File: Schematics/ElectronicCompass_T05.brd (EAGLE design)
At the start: 100 x 80 mm, 59 parts, among them Q1 SPB80P06P, Q2 SPB80P06P, Q3 SPB80P06P, Q4 SPB80P06P, U1 ATMEGA32U4, X1 USBSMD

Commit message: Last minute changes to schematic before the layout begins
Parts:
- added TP26, TP27, TP28: TPTP06R, testpad:TP06R
- C12: value 1uF -> 10uF
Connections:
- new net N$37: Q3.1, U1.8
- new net N$38: TP26.TP, U1.32
- new net N$40: TP28.TP, U1.11
- net N$39: now also TP27.TP; no longer Q3.1
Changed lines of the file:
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@@
 <element name="Q1" library="transistor-fet" package="TO263" value="SPB80P06P" x="35.56" y="52.705"/>
 <element name="Q2" library="transistor-fet" package="TO263" value="SPB80P06P" x="25.4" y="55.245"/>
-<element name="C12" library="rcl" package="C0805" value="1uF" x="18.415" y="31.115"/>
+<element name="C12" library="rcl" package="C0805" value="10uF" x="18.415" y="31.115"/>
 <element name="G1" library="battery" package="SL-340/SM3.6V" value="SL340SM" x="85.09" y="30.48"/>
 <element name="C4" library="rcl" package="C0805" value="1uF" x="42.545" y="39.37"/>
@@
 <element name="U$1" library="LTC4067" package="DFN-12" value="LTC4067" x="-17.78" y="-89.535"/>
 <element name="C3" library="rcl" package="C0805" value="0.1uF" x="-19.05" y="-96.52"/>
+<element name="TP26" library="testpad" package="TP06R" value="TPTP06R" x="-20.32" y="-102.235">
+<attribute name="TP_SIGNAL_NAME" value="" x="-20.32" y="-102.235" size="1.778" layer="27" display="off"/>
+</element>
+<element name="TP27" library="testpad" package="TP06R" value="TPTP06R" x="-20.32" y="-105.41">
+<attribute name="TP_SIGNAL_NAME" value="" x="-20.32" y="-105.41" size="1.778" layer="27" display="off"/>
+</element>
+<element name="TP28" library="testpad" package="TP06R" value="TPTP06R" x="-20.32" y="-108.585">
+<attribute name="TP_SIGNAL_NAME" value="" x="-20.32" y="-108.585" size="1.778" layer="27" display="off"/>
+</element>
 </elements>
 <signals>
@@
 <wire x1="9.525" y1="-15.24" x2="55.92" y2="28.35" width="0" layer="19" extent="1-1"/>
 </signal>
-<signal name="N$39">
-<contactref element="U1" pad="22"/>
-<contactref element="Q3" pad="1"/>
-<wire x1="0.635" y1="-30.73" x2="60.92" y2="28.35" width="0" layer="19" extent="1-1"/>
-</signal>
 <signal name="N$27">
 <contactref element="U1" pad="30"/>
@@
 <wire x1="39.05" y1="47.625" x2="-18.53" y2="-90.885" width="0" layer="19" extent="1-1"/>
 </signal>
+<signal name="N$37">
+<contactref element="U1" pad="8"/>
+<contactref element="Q3" pad="1"/>
+<wire x1="0.635" y1="-30.73" x2="55.02" y2="30.75" width="0" layer="19" extent="1-1"/>
+</signal>
+<signal name="N$38">
+<contactref element="U1" pad="32"/>
+<contactref element="TP26" pad="TP"/>
+<wire x1="61.82" y1="33.75" x2="-20.32" y2="-102.235" width="0" layer="19" extent="1-1"/>
+</signal>
+<signal name="N$39">
+<contactref element="U1" pad="22"/>
+<contactref element="TP27" pad="TP"/>
+<wire x1="60.92" y1="28.35" x2="-20.32" y2="-105.41" width="0" layer="19" extent="1-1"/>
+</signal>
+<signal name="N$40">
+<contactref element="U1" pad="11"/>
+<contactref element="TP28" pad="TP"/>
+<wire x1="55.02" y1="29.25" x2="-20.32" y2="-108.585" width="0" layer="19" extent="1-1"/>
+</signal>
 </signals>

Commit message: Board layout changes
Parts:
- removed JP4: LOGO-SFENEW, SparkFun:SFE-NEW-WEBLOGO
- removed JP5: LOGO-SFESK, SparkFun:SFE-LOGO-FLAME
- moved TP25 135.8 mm to (5.08, 49.5)
- moved U$1 134.8 mm to (29.2, 36.8), turned to 270 degrees
- moved TP24 133.7 mm to (23.5, 47.6), flipped to the bottom, turned to 180 degrees
- moved TP23 133.0 mm to (21.6, 52.1), turned to 180 degrees
- moved C3 132.8 mm to (15.2, 31.8), turned to 180 degrees
- moved TP26 131.2 mm to (38.1, 15.2)
- moved TP28 128.7 mm to (29.2, 10.2)
- moved TP22 128.4 mm to (24.1, 50.2), turned to 180 degrees
- moved TP21 128.3 mm to (26.7, 52.7), turned to 180 degrees
- moved S2 127.8 mm to (8.89, 54.0), flipped to the bottom, turned to 90 degrees
- moved TP27 126.9 mm to (36.2, 8.26)
- moved C2 126.3 mm to (28.6, 29.2)
- moved TP19 123.8 mm to (31.8, 53.3), turned to 180 degrees
- moved TP20 123.2 mm to (29.2, 50.2), turned to 180 degrees
- moved TP17 119.6 mm to (34.3, 51.4), turned to 180 degrees
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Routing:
- added copper zone on layer 1, net GND
- added copper zone on layer 16, net GND
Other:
- board size 100 x 80 mm -> 63.2 x 61 mm

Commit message: board layout continued
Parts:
- moved R8 26.2 mm to (60.3, 15.2), turned to 270 degrees
- moved TP24 23.9 mm to (1.27, 38.7)
- moved C10 23.9 mm to (36.8, 38.7), turned to 0 degrees
- moved R6 22.3 mm to (36.2, 34.9), turned to 0 degrees
- moved R7 21.6 mm to (18.4, 2.54), turned to 90 degrees
- moved C4 19.3 mm to (27.3, 12.7), turned to 180 degrees
- moved C3 18.7 mm to (30.5, 21.0), turned to 90 degrees
- moved C12 16.5 mm to (30.5, 26.7)
- moved S2 15.4 mm to (6.99, 38.7), turned to 180 degrees
- moved S1 15.3 mm to (6.35, 27.9)
- moved R1 13.6 mm to (19.1, 12.7), turned to 90 degrees
- moved X1 8.35 mm to (6.35, 19.1)
- moved TP25 7.41 mm to (1.27, 43.2), flipped to the bottom, turned to 180 degrees
- moved C5 5.24 mm to (27.3, 40.0)
- moved R2 5.12 mm to (20.3, 15.9)
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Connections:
- net GND: no longer U$1.P13, U$1.P3
- net N$16: now also U$1.P10; no longer U$1.P9
- net N$4: no longer U$1.P1
- net N$5: now also U$1.P9; no longer U$1.P10
- net VCC: no longer U$1.P4, U$1.P5

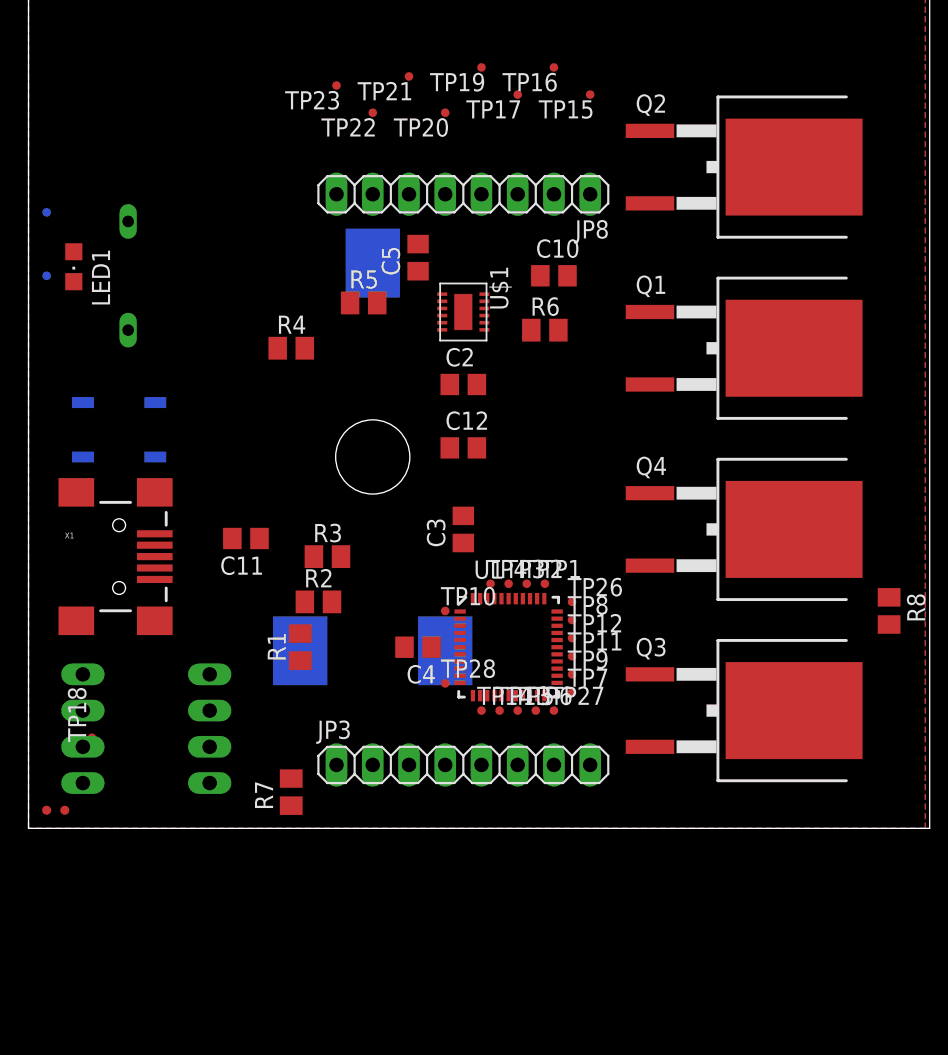
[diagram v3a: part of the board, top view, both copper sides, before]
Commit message: New transistors
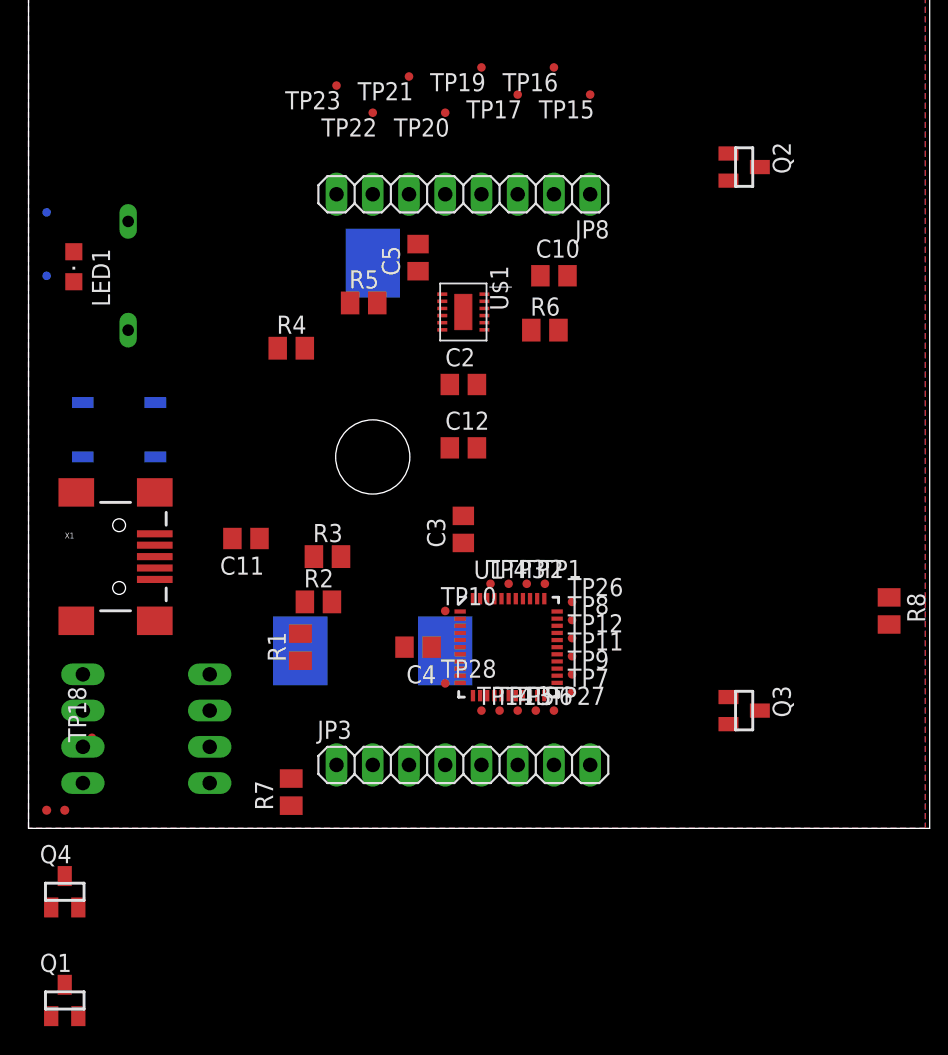
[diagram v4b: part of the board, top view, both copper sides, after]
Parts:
- Q1, Q2, Q3, Q4: value SPB80P06P -> FDN360P; device transistor-fet:TO263 -> transistor-power:SUPER-SOT3
- moved Q1 66.0 mm to (2.54, -12.1), turned to 0 degrees
- moved Q4 54.0 mm to (2.54, -4.45), turned to 0 degrees
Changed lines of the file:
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@@
 <element name="C11" library="rcl" package="C0805" value="1uF" x="15.24" y="20.32" rot="R180"/>
 <element name="LED1" library="led" package="CHIPLED_0805" value="1" x="3.175" y="39.37" rot="R180"/>
-<element name="Q1" library="transistor-fet" package="TO263" value="SPB80P06P" x="50.165" y="33.655" rot="R270"/>
-<element name="Q2" library="transistor-fet" package="TO263" value="SPB80P06P" x="50.165" y="46.355" rot="R270"/>
+<element name="Q2" library="transistor-power" package="SUPER-SOT3" value="FDN360P" x="50.165" y="46.355" rot="R270"/>
 <element name="C12" library="rcl" package="C0805" value="10uF" x="30.48" y="26.67"/>
 <element name="G1" library="battery" package="SL-340/SM3.6V" value="SL340SM" x="24.13" y="26.035" rot="MR0"/>
@@
 <attribute name="TP_SIGNAL_NAME" value="" x="4.445" y="6.35" size="1.778" layer="27" rot="R90" display="off"/>
 </element>
-<element name="Q3" library="transistor-fet" package="TO263" value="SPB80P06P" x="50.165" y="8.255" rot="R270"/>
-<element name="Q4" library="transistor-fet" package="TO263" value="SPB80P06P" x="50.165" y="20.955" rot="R270"/>
+<element name="Q3" library="transistor-power" package="SUPER-SOT3" value="FDN360P" x="50.165" y="8.255" rot="R270"/>
 <element name="R7" library="rcl" package="M0805" value="1M" x="18.415" y="2.54" rot="R90"/>
 <element name="R8" library="rcl" package="M0805" value="1M" x="60.325" y="15.24" rot="R270"/>
@@
 </element>
 <element name="U$1" library="LTC4067" package="DFN-12" value="LTC4067" x="30.48" y="36.195" rot="R270"/>
+<element name="Q4" library="transistor-power" package="SUPER-SOT3" value="FDN360P" x="2.54" y="-4.445"/>
+<element name="Q1" library="transistor-power" package="SUPER-SOT3" value="FDN360P" x="2.54" y="-12.065"/>
 </elements>
 <signals>
@@
 <contactref element="U1" pad="24"/>
 <contactref element="U1" pad="44"/>
-<contactref element="Q4" pad="2"/>
 <contactref element="Q3" pad="2"/>
 <contactref element="S2" pad="2"/>
-<wire x1="36.155" y1="16.1" x2="43.565" y2="18.415" width="0" layer="19" extent="1-1"/>
+<contactref element="Q4" pad="2"/>
 <wire x1="31.155" y1="16.1" x2="36.155" y2="16.1" width="0" layer="19" extent="1-1"/>
 <wire x1="37.055" y1="10.7" x2="36.155" y2="16.1" width="0" layer="19" extent="1-1"/>
 <wire x1="32.155" y1="9.3" x2="37.055" y2="10.7" width="0" layer="19" extent="1-1"/>
+<wire x1="49.065" y1="7.305" x2="37.055" y2="10.7" width="0" layer="19" extent="1-1"/>
 <wire x1="19.05" y1="13.65" x2="31.155" y2="16.1" width="0" layer="19" extent="1-1"/>
-<wire x1="43.565" y1="5.715" x2="37.055" y2="10.7" width="0" layer="19" extent="1-1"/>
 <wire x1="6.985" y1="34.925" x2="19.05" y2="13.65" width="0" layer="19" extent="1-1"/>
+<wire x1="3.49" y1="-5.545" x2="19.05" y2="13.65" width="0" layer="19" extent="1-1"/>
 </signal>
 <signal name="AREF">
@@
 <contactref element="R7" pad="2"/>
 <contactref element="Q3" pad="3"/>
-<wire x1="39.37" y1="4.445" x2="53.665" y2="8.255" width="0" layer="19" extent="1-1"/>
+<wire x1="39.37" y1="4.445" x2="51.265" y2="8.255" width="0" layer="19" extent="1-1"/>
 <wire x1="18.415" y1="3.49" x2="39.37" y2="4.445" width="0" layer="19" extent="1-1"/>
 <wire x1="12.7" y1="3.175" x2="18.415" y2="3.49" width="0" layer="19" extent="1-1"/>
@@
 <contactref element="U1" pad="30"/>
 <contactref element="Q4" pad="1"/>
-<wire x1="37.055" y1="13.7" x2="43.565" y2="23.495" width="0" layer="19" extent="1-1"/>
+<wire x1="1.59" y1="-5.545" x2="37.055" y2="13.7" width="0" layer="19" extent="1-1"/>
 </signal>
 <signal name="LCD_BKLT">
@@
 <contactref element="JP3" pad="1"/>
 <contactref element="Q4" pad="3"/>
-<wire x1="60.325" y1="14.29" x2="53.665" y2="20.955" width="0" layer="19" extent="1-1"/>
-<wire x1="21.59" y1="4.445" x2="53.665" y2="20.955" width="0" layer="19" extent="1-1"/>
+<wire x1="21.59" y1="4.445" x2="60.325" y2="14.29" width="0" layer="19" extent="1-1"/>
+<wire x1="2.54" y1="-3.345" x2="21.59" y2="4.445" width="0" layer="19" extent="1-1"/>
 </signal>
 <signal name="N$2">
@@
 </signal>
 <signal name="N$6">
-<contactref element="Q1" pad="3"/>
 <contactref element="LED1" pad="A"/>
 <contactref element="C5" pad="1"/>
 <contactref element="U$1" pad="P12"/>
-<wire x1="31.957" y1="37.445" x2="53.665" y2="33.655" width="0" layer="19" extent="1-1"/>
+<contactref element="Q1" pad="3"/>
 <wire x1="27.305" y1="39.055" x2="31.957" y2="37.445" width="0" layer="19" extent="1-1"/>
 <wire x1="3.175" y1="40.42" x2="27.305" y2="39.055" width="0" layer="19" extent="1-1"/>
+<wire x1="2.54" y1="-10.965" x2="3.175" y2="40.42" width="0" layer="19" extent="1-1"/>
 </signal>
 <signal name="N$8">
@@
 </signal>
 <signal name="N$9">
-<contactref element="Q1" pad="1"/>
 <contactref element="C2" pad="2"/>
 <contactref element="U$1" pad="P7"/>
-<wire x1="31.957" y1="34.945" x2="43.565" y2="36.195" width="0" layer="19" extent="1-1"/>
+<contactref element="Q1" pad="1"/>
 <wire x1="31.43" y1="31.115" x2="31.957" y2="34.945" width="0" layer="19" extent="1-1"/>
+<wire x1="1.59" y1="-13.165" x2="31.43" y2="31.115" width="0" layer="19" extent="1-1"/>
 </signal>
 <signal name="N$11">
-<contactref element="Q1" pad="2"/>
 <contactref element="C11" pad="1"/>
 <contactref element="C2" pad="1"/>
@@
 <contactref element="U1" pad="7"/>
 <contactref element="U$1" pad="P6"/>
-<wire x1="29.53" y1="31.115" x2="43.565" y2="31.115" width="0" layer="19" extent="1-1"/>
-<wire x1="29.003" y1="34.945" x2="29.53" y2="31.115" width="0" layer="19" extent="1-1"/>
+<contactref element="Q1" pad="2"/>
+<wire x1="29.53" y1="31.115" x2="29.003" y2="34.945" width="0" layer="19" extent="1-1"/>
 <wire x1="29.53" y1="26.67" x2="29.53" y2="31.115" width="0" layer="19" extent="1-1"/>
 <wire x1="30.255" y1="14.7" x2="29.53" y2="26.67" width="0" layer="19" extent="1-1"/>
@@
 <wire x1="16.19" y1="20.32" x2="29.53" y2="26.67" width="0" layer="19" extent="1-1"/>
 <wire x1="8.85" y1="20.65" x2="16.19" y2="20.32" width="0" layer="19" extent="1-1"/>
+<wire x1="3.49" y1="-13.165" x2="8.85" y2="20.65" width="0" layer="19" extent="1-1"/>
 </signal>
 <signal name="N$5">
@@
 <contactref element="Q2" pad="3"/>
 <contactref element="U$1" pad="P9"/>
-<wire x1="31.957" y1="35.945" x2="53.665" y2="46.355" width="0" layer="19" extent="1-1"/>
+<wire x1="31.957" y1="35.945" x2="51.265" y2="46.355" width="0" layer="19" extent="1-1"/>
 <wire x1="24.13" y1="39.624" x2="31.957" y2="35.945" width="0" layer="19" extent="1-16"/>
 <wire x1="1.27" y1="38.735" x2="24.13" y2="39.624" width="0" layer="19" extent="16-16"/>
@@
 <contactref element="Q2" pad="1"/>
 <contactref element="U$1" pad="P10"/>
-<wire x1="31.957" y1="36.445" x2="43.565" y2="48.895" width="0" layer="19" extent="1-1"/>
+<wire x1="31.957" y1="36.445" x2="49.065" y2="47.305" width="0" layer="19" extent="1-1"/>
 </signal>
 <signal name="N$36">
@@
 <contactref element="C10" pad="1"/>
 <contactref element="U$1" pad="P11"/>
-<wire x1="35.88" y1="38.735" x2="43.565" y2="43.815" width="0" layer="19" extent="1-1"/>
+<wire x1="35.88" y1="38.735" x2="49.065" y2="45.405" width="0" layer="19" extent="1-1"/>
 <wire x1="31.957" y1="36.945" x2="35.88" y2="38.735" width="0" layer="19" extent="1-1"/>
 <wire x1="6.985" y1="42.545" x2="31.957" y2="36.945" width="0" layer="19" extent="1-1"/>
@@
 <contactref element="U1" pad="8"/>
 <contactref element="Q3" pad="1"/>
-<wire x1="30.255" y1="11.7" x2="43.565" y2="10.795" width="0" layer="19" extent="1-1"/>
+<wire x1="30.255" y1="11.7" x2="49.065" y2="9.205" width="0" layer="19" extent="1-1"/>
 </signal>
 <signal name="N$38">
